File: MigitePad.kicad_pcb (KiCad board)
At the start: 2 copper layers, 139.7 x 114.3 mm, 75 parts, among them SW1 SW_Push, U1 ATmega32U4-AU, Y1 16MHz

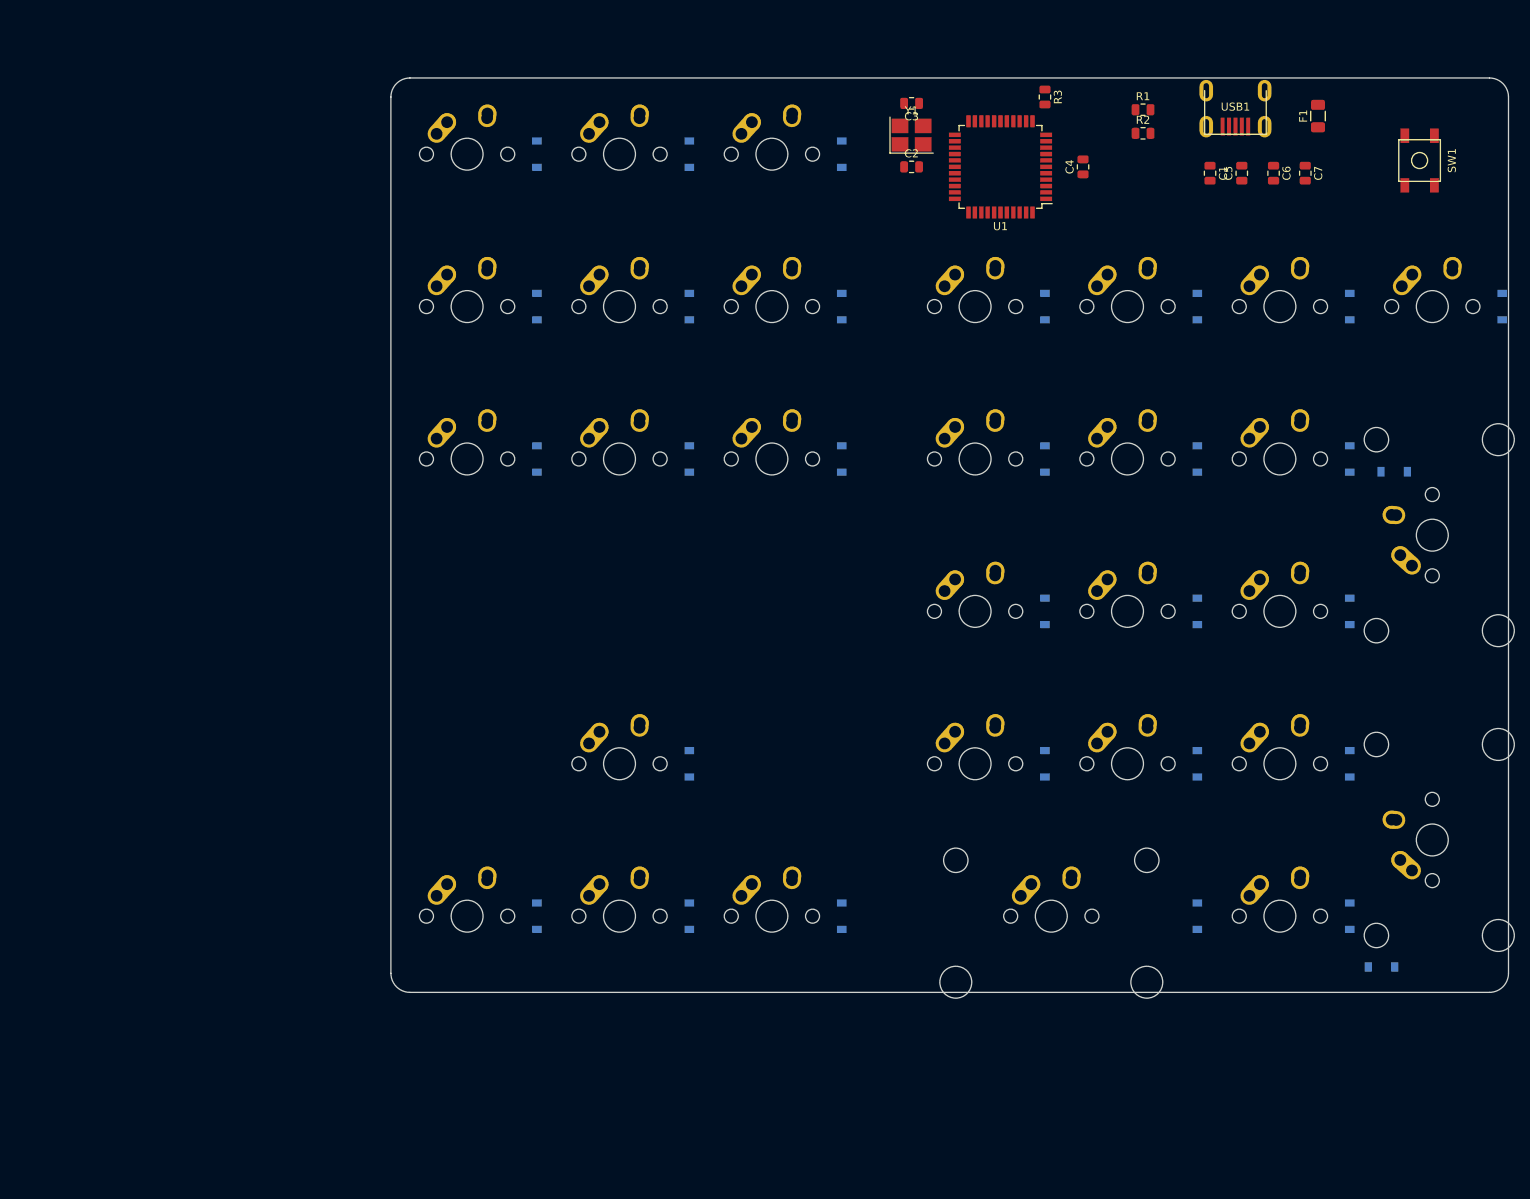
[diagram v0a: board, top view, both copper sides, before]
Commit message: Changed to ProMicro
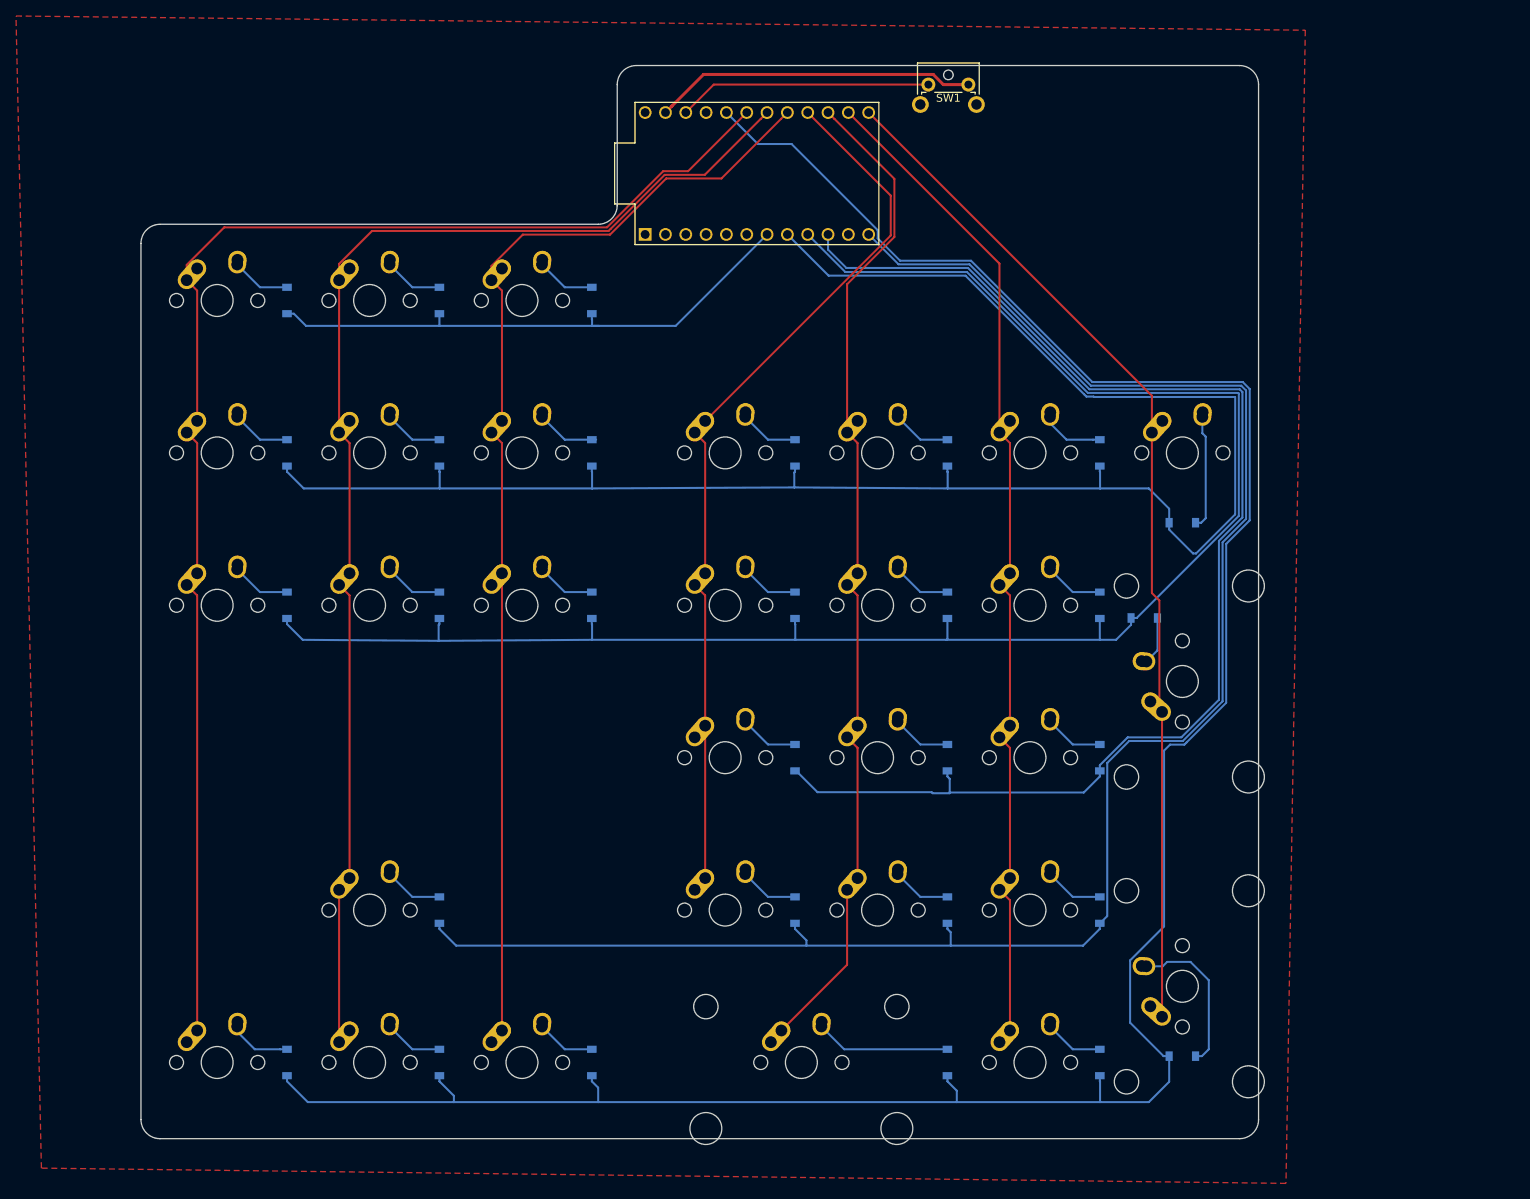
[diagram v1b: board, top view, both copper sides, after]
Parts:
- removed C1, C5, C6: 0.1uF, Capacitor_SMD:C_0805_2012Metric
- removed C2, C3: 22pF, Capacitor_SMD:C_0805_2012Metric
- removed C4: 1uf, Capacitor_SMD:C_0805_2012Metric
- removed C7: 10uF, Capacitor_SMD:C_0805_2012Metric
- removed F1: Polyfuse_Small, Fuse:Fuse_1206_3216Metric
- removed R1, R2: 22, Resistor_SMD:R_0805_2012Metric
- removed R3: 10k, Resistor_SMD:R_0805_2012Metric
- removed USB1: Molex-0548190589, random-keyboard-parts:Molex-0548190589
- removed Y1: 16MHz, Crystal:Crystal_SMD_3225-4Pin_3.2x2.5mm_HandSoldering
- SW1: footprint random-keyboard-parts:SKQG-1155865 -> Keebio-Parts:SW_Tactile_SPST_Angled_MJTP1117
- U1: value ATmega32U4-AU -> ProMicro; footprint Package_QFP:TQFP-44_10x10mm_P0.8mm -> promicro:ProMicro
- moved SW1 62.1 mm to (162.4, 32.6), turned to 0 degrees
- moved D28 48.2 mm to (194.2, 87.3), turned to 0 degrees
- moved D22 36.2 mm to (164.8, 135.8)
- moved MX34 36.2 mm to (137.0, 135.8)
- moved MX60-2u1 36.2 mm to (194.2, 145.3)
- moved D18 36.2 mm to (164.8, 154.8)
- moved D19 36.2 mm to (164.8, 78.6)
- moved D20 36.2 mm to (164.8, 97.7)
- moved D21 36.2 mm to (164.8, 116.7)
- moved MX28 36.2 mm to (137.0, 78.6)
- moved MX30 36.2 mm to (137.0, 97.7)
- moved MX32 36.2 mm to (137.0, 116.7)
- moved MX36 36.2 mm to (146.6, 154.8)
- moved MX56 36.2 mm to (194.2, 78.6)
- moved MX58-2u1 36.2 mm to (194.2, 107.2)
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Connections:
- SW1 pad 1: GND -> Net-(SW1-Pad1)
- SW1 pad 2: Net-(SW1-Pad2) -> GND
- U1 pad 10: Net-(U1-Pad10) -> ROW3
- U1 pad 12: Net-(U1-Pad12) -> ROW4
- U1 pad 13: Net-(SW1-Pad2) -> COL6
- U1 pad 14: +5V -> COL5
- U1 pad 15: GND -> COL4
- U1 pad 16: Net-(C3-Pad1) -> COL3
- U1 pad 17: Net-(C2-Pad1) -> COL2
- U1 pad 18: Net-(U1-Pad18) -> COL1
- U1 pad 19: Net-(U1-Pad19) -> COL0
- U1 pad 2: +5V -> Net-(U1-Pad2)
- U1 pad 20: Net-(U1-Pad20) -> ROW5
- U1 pad 21: Net-(U1-Pad21) -> VCC
- U1 pad 22: Net-(U1-Pad22) -> Net-(SW1-Pad1)
- U1 pad 24: +5V -> Net-(U1-Pad24)
- U1 pad 3: Net-(R1-Pad1) -> GND
- U1 pad 4: Net-(R2-Pad1) -> GND
- U1 pad 5: GND -> Net-(U1-Pad5)
- U1 pad 7: +5V -> ROW0
- U1 pad 8: Net-(U1-Pad8) -> ROW1
- U1 pad 9: Net-(U1-Pad9) -> ROW2
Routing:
- net ROW5: track 0.00 -> 304.5 mm
- net ROW4: track 0.00 -> 225.4 mm
- net ROW1: track 0.00 -> 220.0 mm
- net ROW2: track 0.00 -> 218.6 mm
- net COL0: track 0.00 -> 173.1 mm
- net ROW3: track 0.00 -> 163.5 mm
- net COL1: track 0.00 -> 158.8 mm
- net COL2: track 0.00 -> 144.1 mm
- net COL5: track 0.00 -> 128.4 mm
- net COL6: track 0.00 -> 128.2 mm
- net COL4: track 0.00 -> 125.3 mm
- net COL3: track 0.00 -> 109.8 mm
- net ROW0: track 0.00 -> 69.1 mm
- net GND: track 0.00 -> 40.4 mm
- net Net-(SW1-Pad1): track 0.00 -> 31.8 mm
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- added copper zone on F.Cu, net GND
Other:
- board size 139.7 x 114.3 mm -> 139.7 x 134.1 mm
- net class Default: trace_width 0.25 -> 0.254
- net class Power added: clearance 0.2, trace_width 0.381, via_dia 0.8, via_drill 0.4

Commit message: Removed GND fill
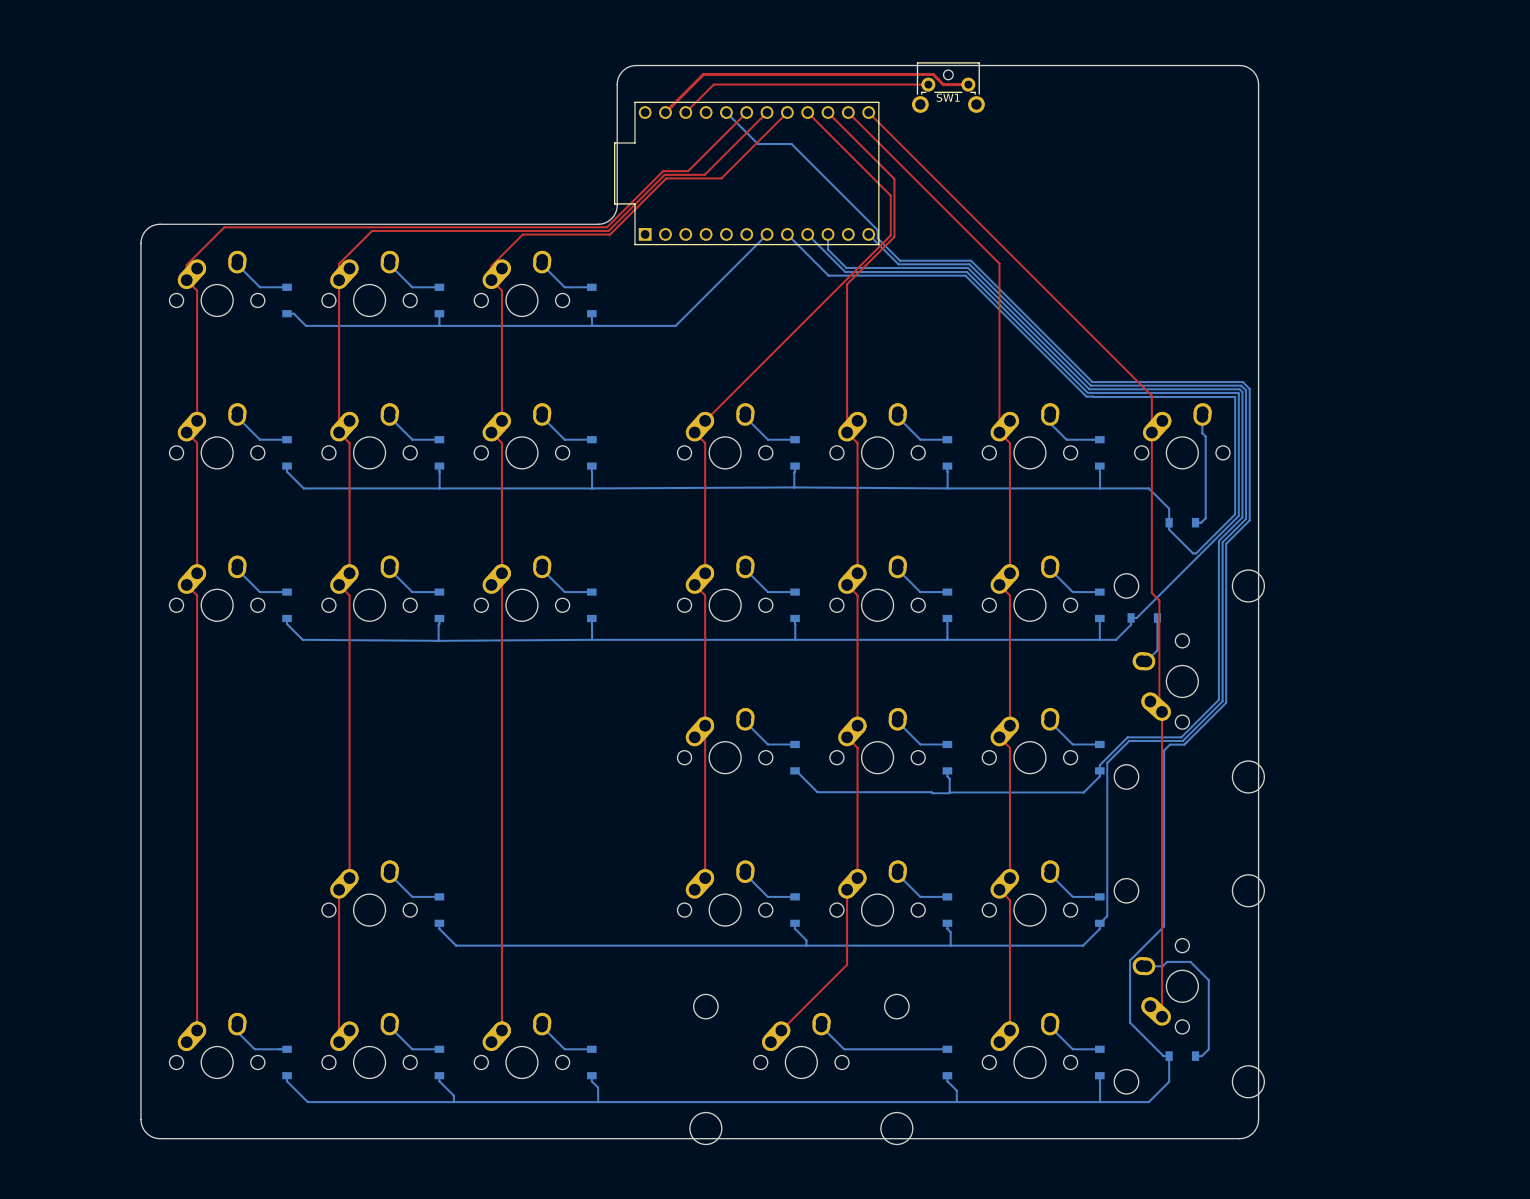
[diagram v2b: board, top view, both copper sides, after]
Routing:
- removed copper zone on F.Cu, net GND
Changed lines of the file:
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@@
   (page A4)
   (layers
-    (0 F.Cu signal hide)
+    (0 F.Cu signal)
     (31 B.Cu signal)
     (32 B.Adhes user)
@@
   (segment (start 164.305942 32.5755) (end 163.040441 31.309999) (width 0.381) (layer F.Cu) (net 51))
   (segment (start 167.433 32.5755) (end 164.305942 32.5755) (width 0.381) (layer F.Cu) (net 51))
-  (zone (net 51) (net_name GND) (layer F.Cu) (hatch edge 0.508)
-    (connect_pads (clearance 0.508))
-    (min_thickness 0.254)
-    (fill yes (arc_segments 32) (thermal_gap 0.508) (thermal_bridge_width 0.508) (smoothing chamfer))
-    (polygon
-      (pts
-        (xy 209.55 25.781) (xy 207.137 169.926) (xy 51.562 168.021) (xy 48.387 24.003)
-      )
-    )
-  )
 )

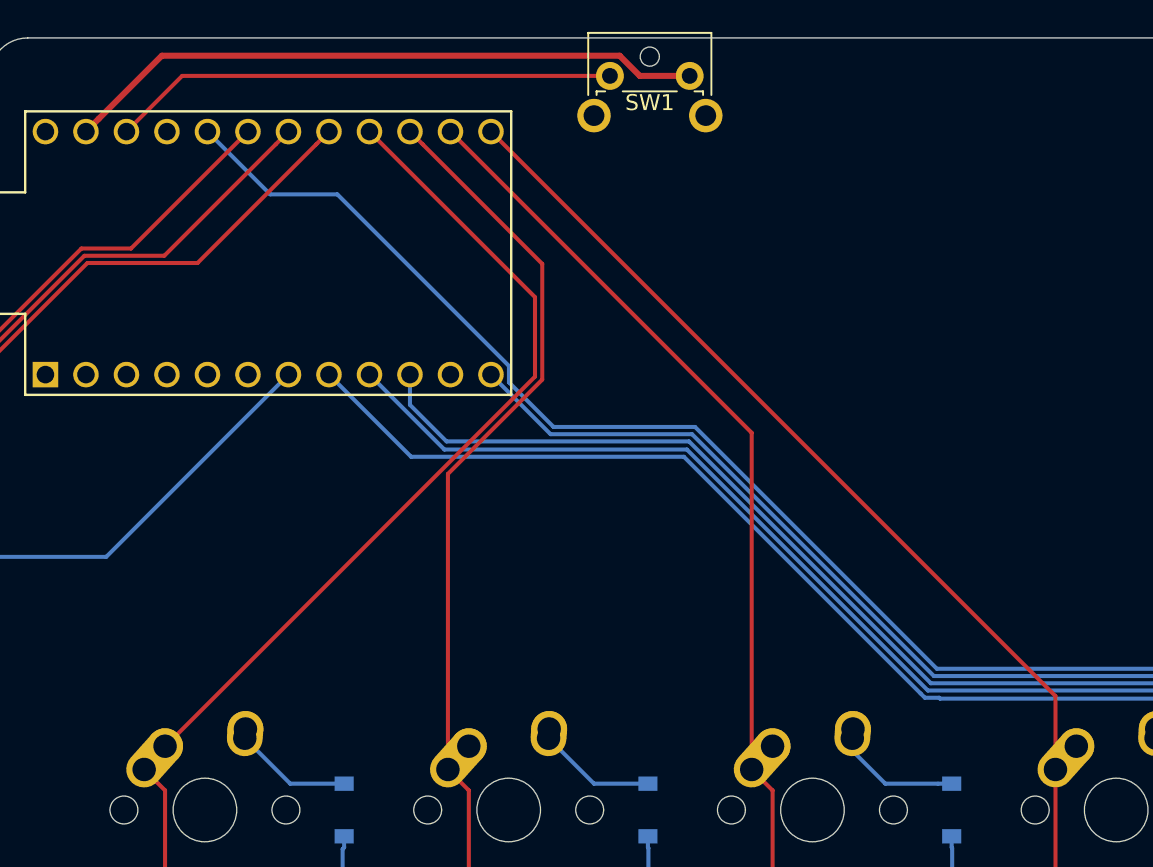
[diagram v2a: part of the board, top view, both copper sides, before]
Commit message: Added OLED header
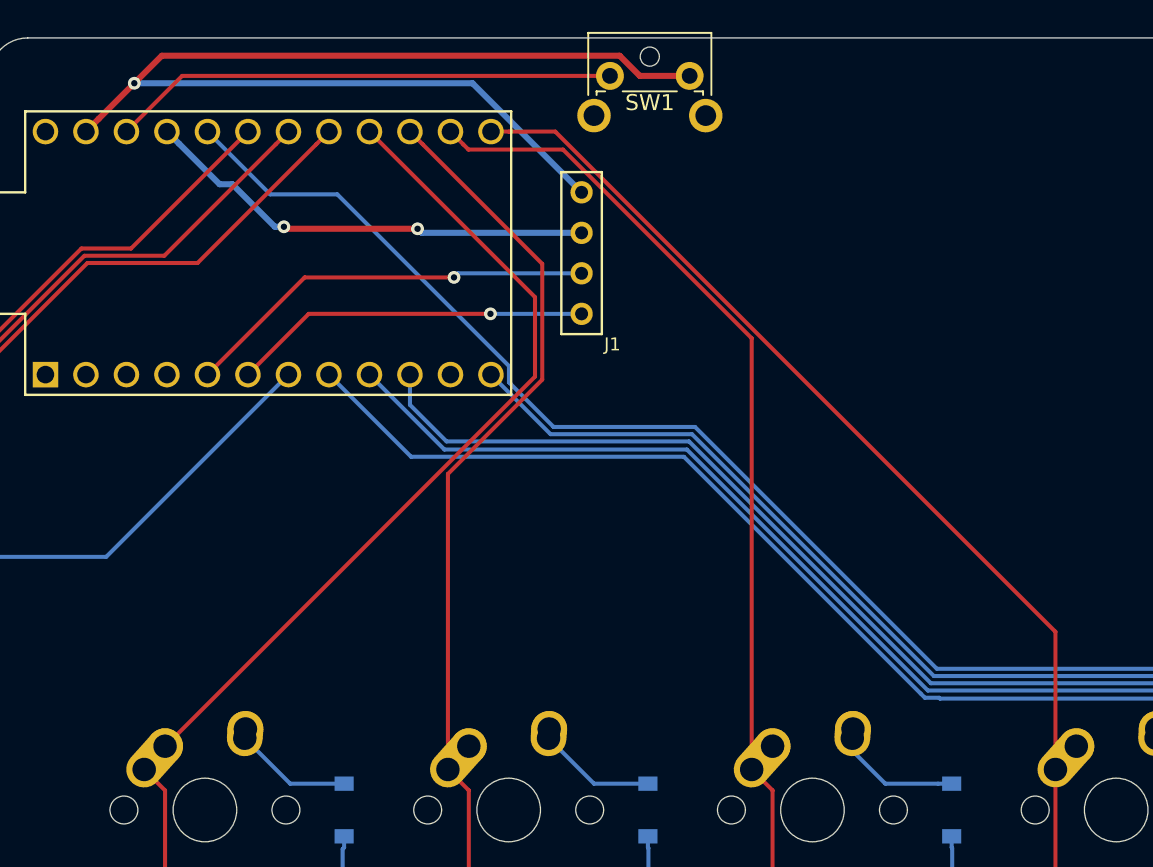
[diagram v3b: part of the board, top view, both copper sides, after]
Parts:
- added J1: OLED, Lily58-footprint:MY_SIL-4, F.Cu at (160.7, 47.5)
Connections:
- U1 pad 5: Net-(U1-Pad5) -> SCL
- U1 pad 6: Net-(U1-Pad6) -> SDA
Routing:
- net GND: track 40.4 -> 71.2 mm, vias 0 -> 1
- net VCC: track 0.00 -> 28.6 mm, vias 0 -> 2
- net SCL: track 0.00 -> 26.1 mm, vias 0 -> 1
- net SDA: track 0.00 -> 22.5 mm, vias 0 -> 1
- net COL5: track 128.4 -> 131.8 mm
- net COL6: track 128.2 -> 130.6 mm
